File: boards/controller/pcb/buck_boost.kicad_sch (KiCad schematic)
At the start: 38 parts

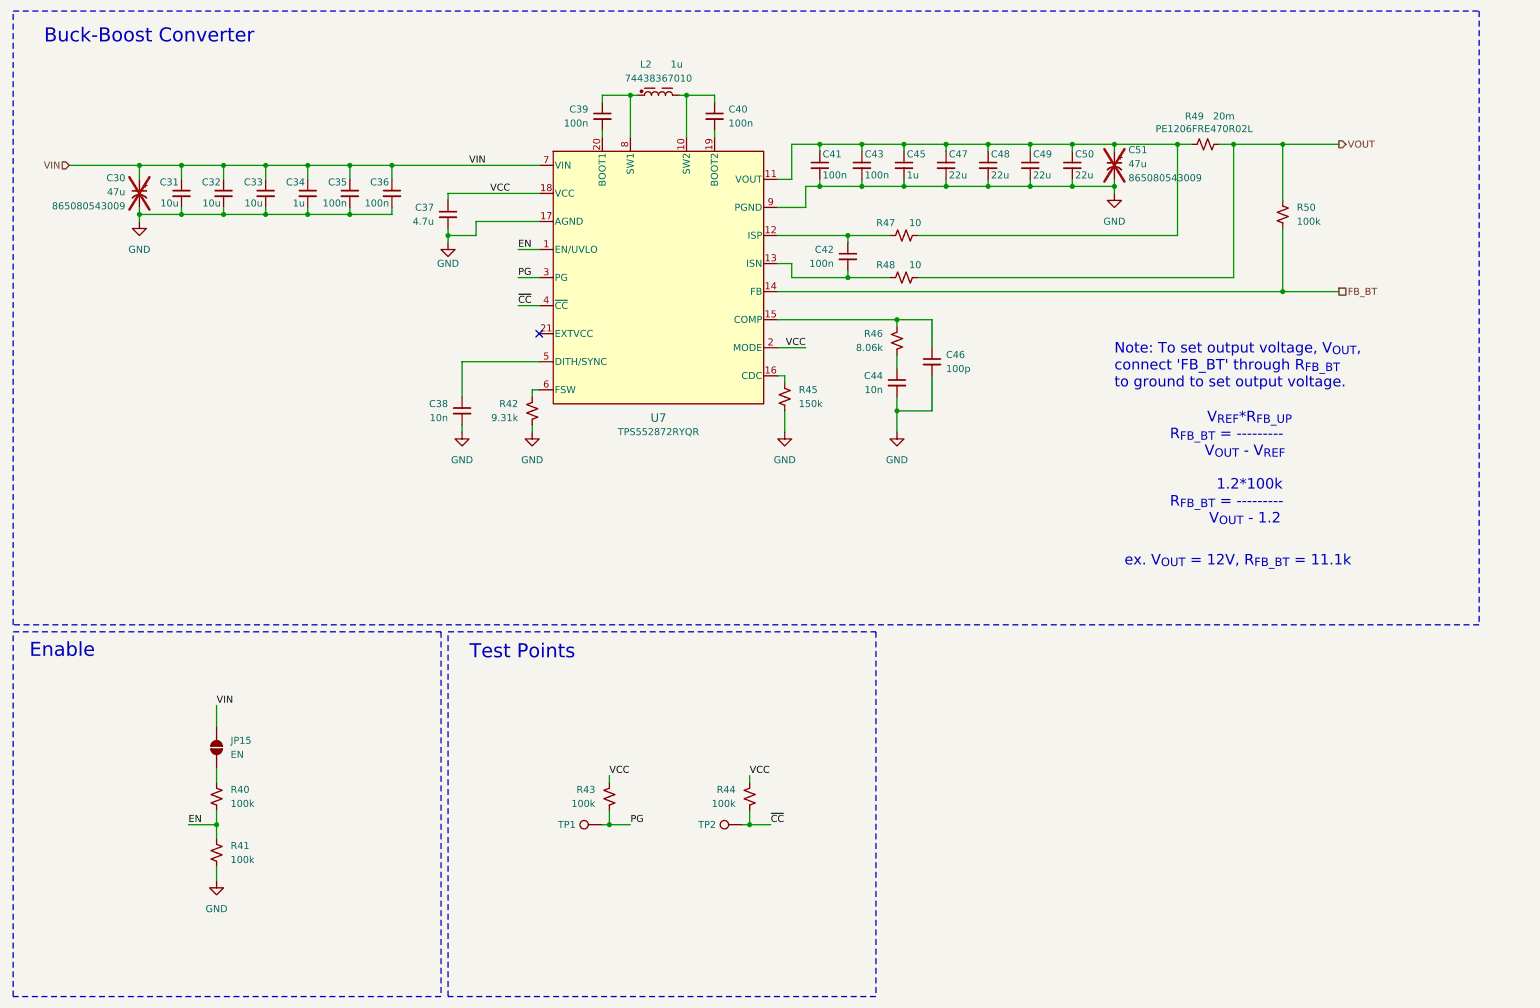
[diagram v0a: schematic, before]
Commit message: controller: Update PCB
Signed-off-by: Nicholas Loehrke <nicholasnloehrke@gmail.com>
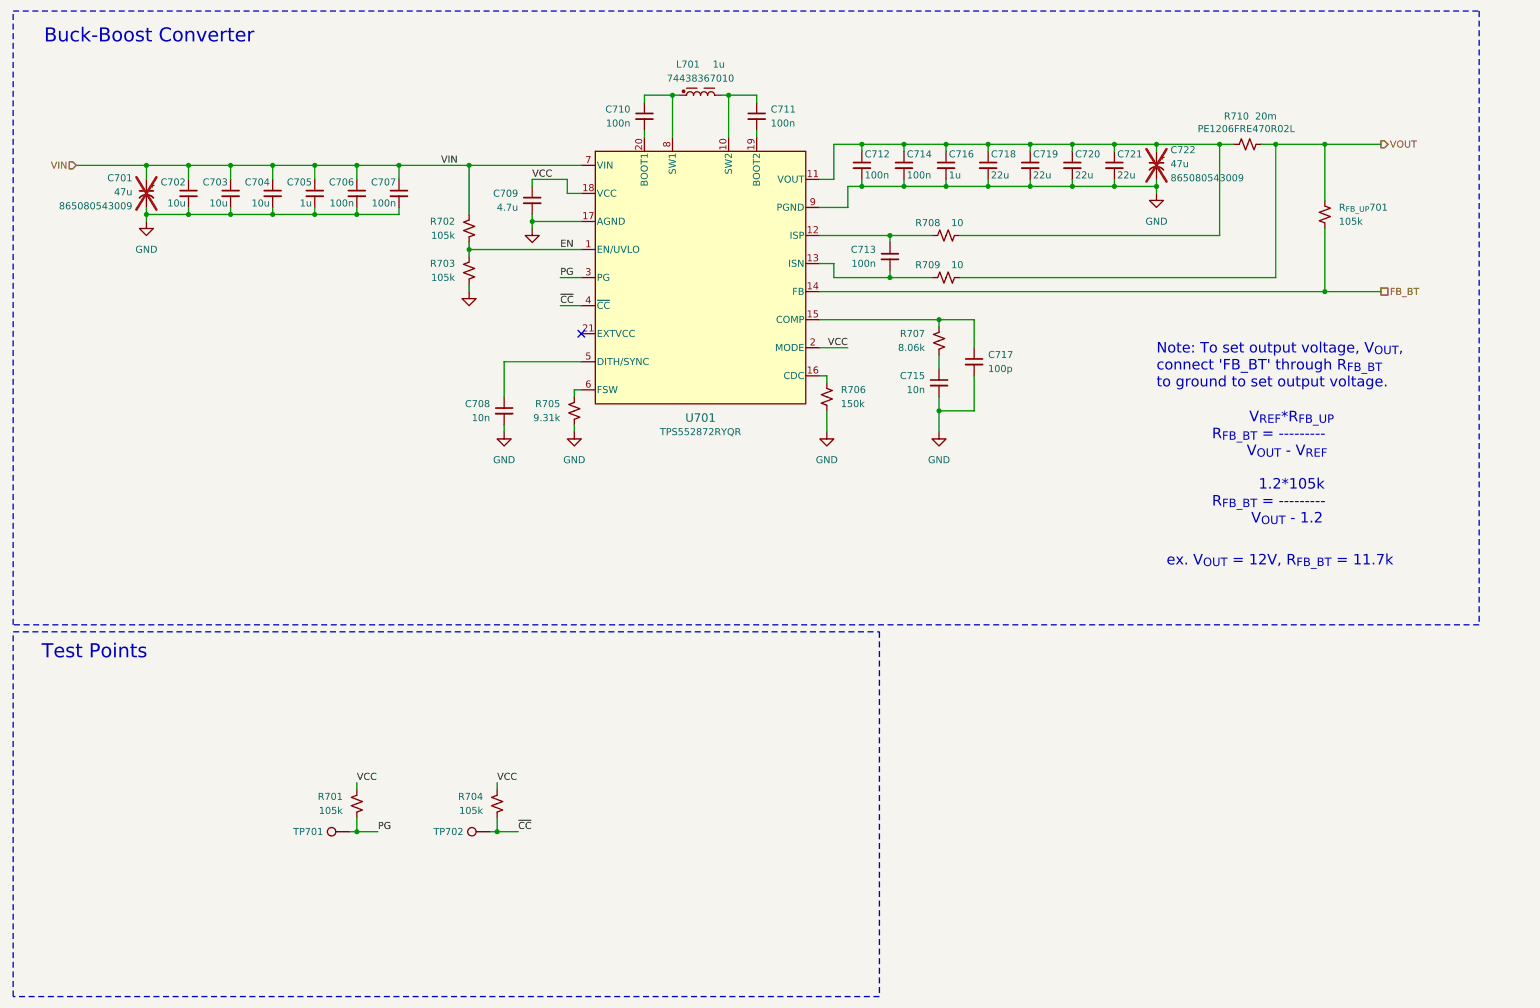
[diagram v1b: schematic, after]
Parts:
- removed JP15: EN, Jumper:SolderJumper-2_P1.3mm_Open_RoundedPad1.0x1.5mm, symbol Jumper:SolderJumper_2_Open
- removed R40, R41: 100k, Resistor_SMD:R_0603_1608Metric, symbol Device:R_Small_US
- added R702, R703: 105k, Resistor_SMD:R_0603_1608Metric, symbol Device:R_Small_US
- R701: renamed from R43; value 100k -> 105k
- R704: renamed from R44; value 100k -> 105k
- R_{FB_UP}701: renamed from R50; value 100k -> 105k
- renumbered C30 to C701, C31 to C702, C32 to C703, C33 to C704, C34 to C705, C35 to C706, C36 to C707, C38 to C708, C37 to C709, C39 to C710, C40 to C711, C41 to C712, C42 to C713, C43 to C714, C44 to C715, C45 to C716, C46 to C717, C47 to C718, C48 to C719, C49 to C720, C50 to C721, C51 to C722, L2 to L701, R42 to R705, R45 to R706, R46 to R707, R47 to R708, R48 to R709, R49 to R710, TP1 to TP701, TP2 to TP702, U7 to U701
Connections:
- net EN: now also R702.2, R703.1
- net GND: now also R703.2
- net VIN: now also R702.1
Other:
- note added: "1.2*105k R_{FB_BT} = --------- V_{OUT} - 1.2"
- note added: "ex. V_{OUT} = 12V, R_{FB_BT} = 11.7k"
- note removed: "1.2*100k R_{FB_BT} = --------- V_{OUT} - 1.2"
- note removed: "Enable"
- note removed: "ex. V_{OUT} = 12V, R_{FB_BT} = 11.1k"
- moved on the sheet: C701, C702, C703, C704, C705, C706, C707, C708, C709, C710, C711, C712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
